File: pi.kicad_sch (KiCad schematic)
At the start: 4 parts

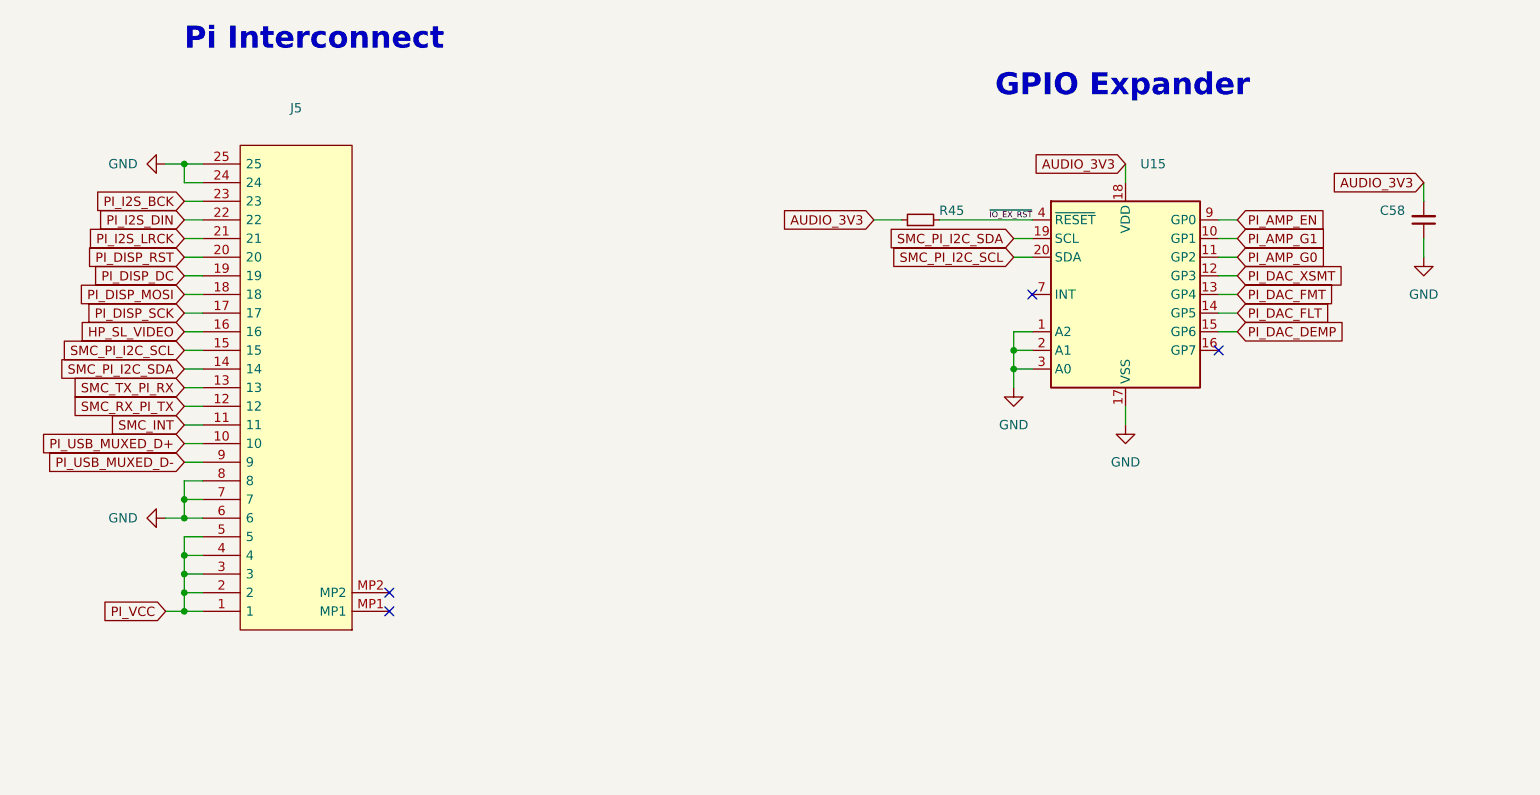
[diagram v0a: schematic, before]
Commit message: layout: add testpoints, extra mounting hole, grounding clips
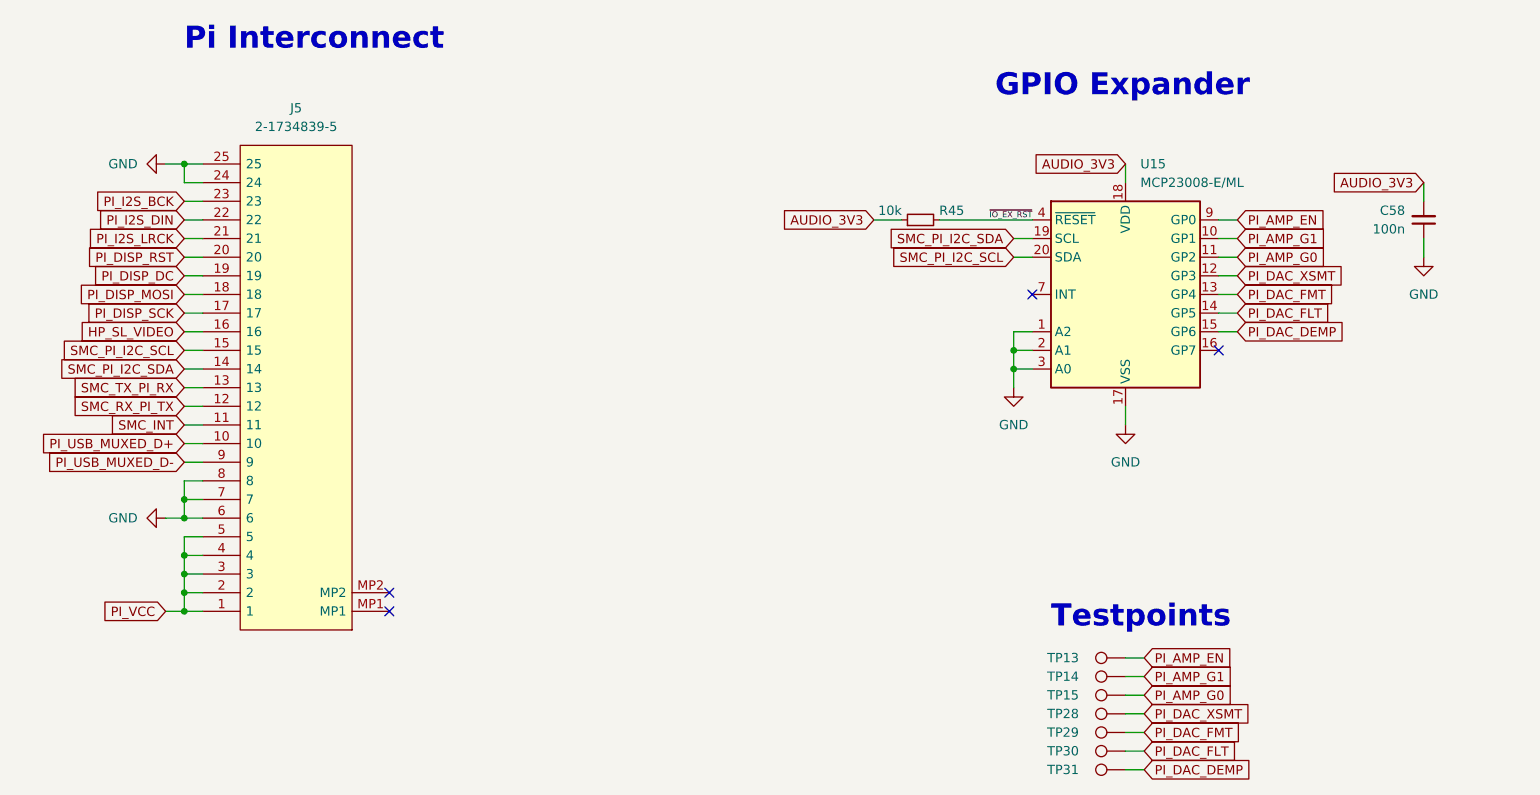
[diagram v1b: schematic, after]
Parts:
- added TP13, TP14, TP15, TP28, TP29, TP30, TP31: TestPoint, TestPoint:TestPoint_Pad_D1.5mm, symbol Connector:TestPoint
- C58: value (none) -> 100n; footprint (none) -> Capacitor_SMD:C_0402_1005Metric
- J5: value (none) -> 2-1734839-5; footprint (none) -> Gigahawk:217348395
- R45: value (none) -> 10k; footprint (none) -> Resistor_SMD:R_0402_1005Metric
- U15: value (none) -> MCP23008-E/ML; footprint (none) -> Package_DFN_QFN:QFN-20-1EP_4x4mm_P0.5mm_EP2.7x2.7mm
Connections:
- net PI_AMP_EN: now also TP13.1
- net PI_AMP_G0: now also TP15.1
- net PI_AMP_G1: now also TP14.1
- net PI_DAC_DEMP: now also TP31.1
- net PI_DAC_FLT: now also TP30.1
- net PI_DAC_FMT: now also TP29.1
- net PI_DAC_XSMT: now also TP28.1
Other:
- note added: "Testpoints"

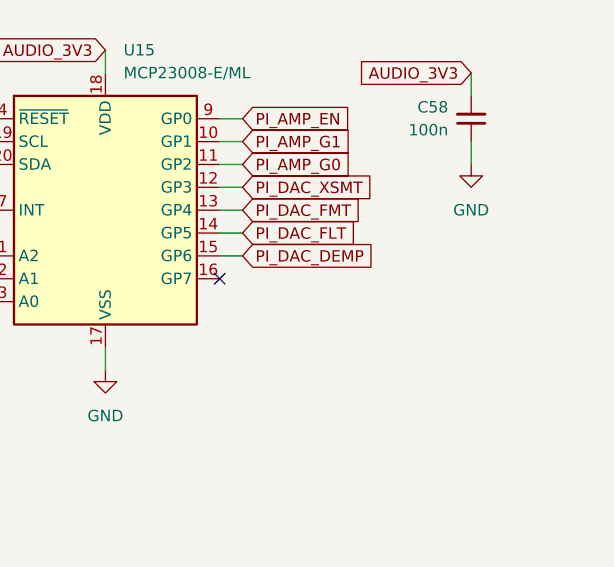
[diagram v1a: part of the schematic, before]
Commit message: schematic: add resistors to allow latching pi power
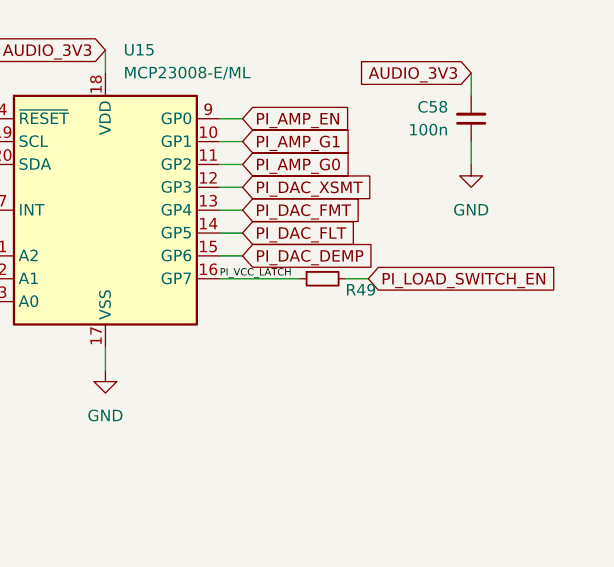
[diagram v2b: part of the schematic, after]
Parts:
- added R49: (no value), Resistor_SMD:R_0402_1005Metric, symbol Device:R_Small
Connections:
- net PI_VCC_LATCH: now reaches U15.16 (GP7)
- net PI_VCC_LATCH: now also R49.1
- new net PI_LOAD_SWITCH_EN: R49.2
- no-connect marks 4 -> 3
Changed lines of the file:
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@@
   (junction (at 40.64 69.85) (diameter 0) (color 0 0 0 0)
   )
-  (no_connect (at 181.61 95.25))
   (no_connect (at 156.21 87.63))
   (no_connect (at 68.58 130.81))
@@
     (stroke (width 0) (type default) (color 0 0 0 0))
   )
+  (wire (pts (xy 195.58 95.25) (xy 198.12 95.25))
+    (stroke (width 0) (type default) (color 0 0 0 0))
+  )
   (wire (pts (xy 43.18 123.19) (xy 40.64 123.19))
     (stroke (width 0) (type default) (color 0 0 0 0))
@@
   )
   (wire (pts (xy 40.64 85.09) (xy 43.18 85.09))
+    (stroke (width 0) (type default) (color 0 0 0 0))
+  )
+  (wire (pts (xy 181.61 95.25) (xy 190.5 95.25))
     (stroke (width 0) (type default) (color 0 0 0 0))
   )
@@
     (effects (font (size 3 3) (thickness 0.6) bold) (justify left bottom))
   )
+  (label "PI_VCC_LATCH" (at 181.61 95.25 0)
+    (effects (font (size 0.8 0.8)) (justify left bottom))
+  )
   (label "~{IO_EX_RST}" (at 156.21 77.47 180)
     (effects (font (size 0.8 0.8)) (justify right bottom))
@@
     (property "Intersheet References" "${INTERSHEET_REFS}" (id 0) (at 135.8959 80.0894 0)
       (effects (font (size 1.27 1.27)) (justify right) hide)
+    )
+  )
+  (global_label "PI_LOAD_SWITCH_EN" (shape input) (at 198.12 95.25 0) (fields_autoplaced)
+    (effects (font (size 1.27 1.27)) (justify left))
+    (property "Intersheet References" "${INTERSHEET_REFS}" (id 0) (at 219.3412 95.1706 0)
+      (effects (font (size 1.27 1.27)) (justify left) hide)
     )
   )
@@
     (pin "1")
   )
+  (symbol (lib_id "Device:R_Small") (at 193.04 95.25 90) (mirror x) (unit 1)
+    (in_bom yes) (on_board yes)
+    (property "Reference" "R49" (id 0) (at 195.58 96.52 90)
+      (effects (font (size 1.27 1.27)) (justify right))
+    )
+    (property "Value" "" (id 1) (at 190.5 96.52 90)
+      (effects (font (size 1.27 1.27)) (justify left))
+    )
+    (property "Footprint" "Resistor_SMD:R_0402_1005Metric" (id 2) (at 193.04 95.25 0)
+      (effects (font (size 1.27 1.27)) hide)
+    )
+    (property "Datasheet" "~" (id 3) (at 193.04 95.25 0)
+      (effects (font (size 1.27 1.27)) hide)
+    )
+    (pin "1")
+    (pin "2")
+  )
   (symbol (lib_id "Connector:TestPoint") (at 168.91 144.78 90) (unit 1)

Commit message: compute: finish layout and routing
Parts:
- R49: value (none) -> 1k
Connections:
- net SMC_RX_PI_TX: now also J5.13; no longer J5.12
- net SMC_TX_PI_RX: now also J5.12; no longer J5.13

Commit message: ci: prepare files for CI
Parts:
- U15: footprint Package_DFN_QFN:QFN-20-1EP_4x4mm_P0.5mm_EP2.7x2.7mm -> Gigahawk:QFN-20-1EP_4x4mm_P0.5mm_EP2.7x2.7mm
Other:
- title: (none) -> piPod IO/SMC Board
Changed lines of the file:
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@@
 (kicad_sch (version 20211123) (generator eeschema)
   (paper "A4")
+  (title_block
+    (title "piPod IO/SMC Board")
+    (date "${DATE}")
+    (rev "%{TAG} (${REVISION})")
+  )
   (junction (at 40.64 128.27) (diameter 0) (color 0 0 0 0)
   )
@@
       (effects (font (size 1.27 1.27)) (justify left))
     )
-    (property "Footprint" "Package_DFN_QFN:QFN-20-1EP_4x4mm_P0.5mm_EP2.7x2.7mm" (id 2) (at 168.91 114.3 0)
-      (effects (font (size 1.27 1.27)) hide)
-    )
+    (property "Footprint" "Gigahawk:QFN-20-1EP_4x4mm_P0.5mm_EP2.7x2.7mm" (id 2) (at 168.91 114.3 0)
+      (effects (font (size 1.27 1.27)) hide)
+    )

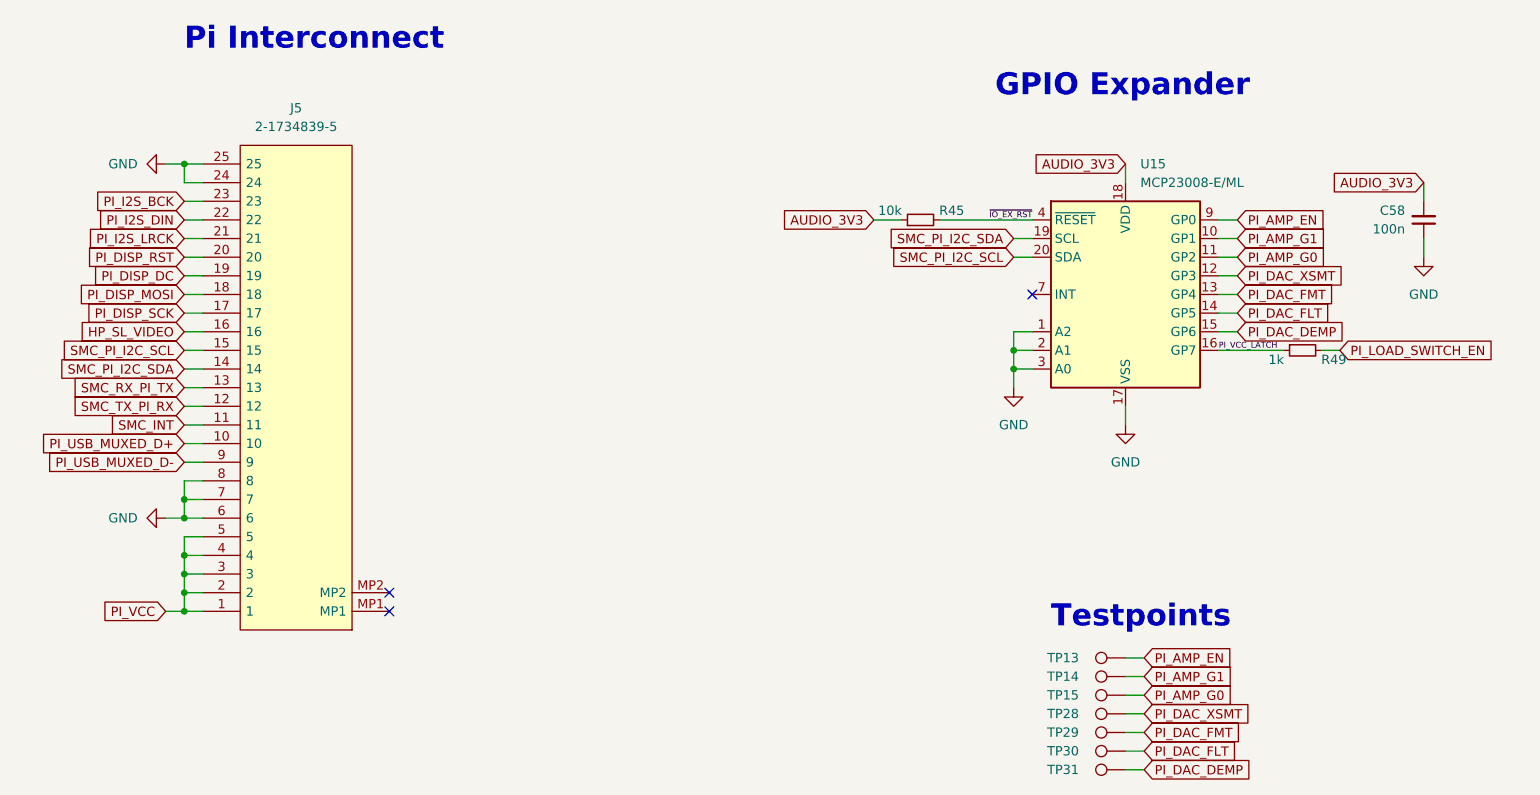
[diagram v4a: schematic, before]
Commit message: ci: test marking parts in sch for bom
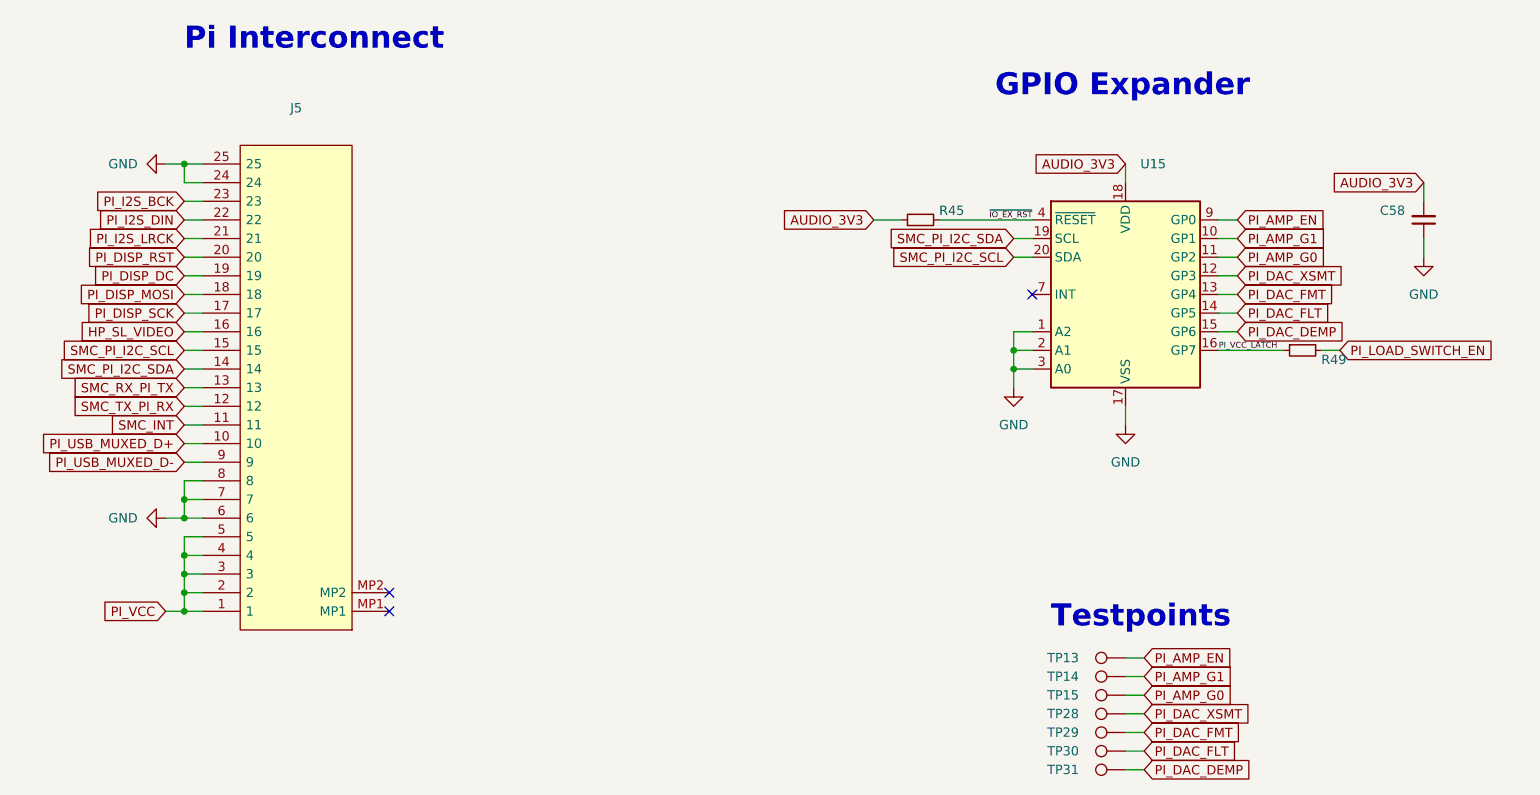
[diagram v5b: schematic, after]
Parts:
- C58: value 100n -> (none); footprint Capacitor_SMD:C_0402_1005Metric -> (none)
- J5: value 2-1734839-5 -> (none); footprint Gigahawk:217348395 -> (none)
- R45: value 10k -> (none); footprint Resistor_SMD:R_0402_1005Metric -> (none)
- R49: value 1k -> (none); footprint Resistor_SMD:R_0402_1005Metric -> (none)
- TP13, TP14, TP15, TP28, TP29, TP30, TP31: value TestPoint -> (none); footprint TestPoint:TestPoint_Pad_D1.5mm -> (none)
- U15: value MCP23008-E/ML -> (none); footprint Gigahawk:QFN-20-1EP_4x4mm_P0.5mm_EP2.7x2.7mm -> (none)
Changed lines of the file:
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@@
       (effects (font (size 1.27 1.27)) (justify right))
     )
-    (property "Value" "10k" (id 1) (at 138.43 76.2 90)
-      (effects (font (size 1.27 1.27)) (justify left))
-    )
-    (property "Footprint" "Resistor_SMD:R_0402_1005Metric" (id 2) (at 140.97 77.47 0)
+    (property "Value" "" (id 1) (at 138.43 76.2 90)
+      (effects (font (size 1.27 1.27)) (justify left))
+    )
+    (property "Footprint" "" (id 2) (at 140.97 77.47 0)
       (effects (font (size 1.27 1.27)) hide)
     )
@@
       (effects (font (size 1.27 1.27)) (justify left))
     )
-    (property "Value" "TestPoint" (id 1) (at 166.8779 147.32 0)
-      (effects (font (size 1.27 1.27)) (justify left) hide)
-    )
-    (property "Footprint" "TestPoint:TestPoint_Pad_D1.5mm" (id 2) (at 168.91 144.78 0)
+    (property "Value" "" (id 1) (at 166.8779 147.32 0)
+      (effects (font (size 1.27 1.27)) (justify left) hide)
+    )
+    (property "Footprint" "" (id 2) (at 168.91 144.78 0)
       (effects (font (size 1.27 1.27)) hide)
     )
@@
       (effects (font (size 1.27 1.27)) (justify left))
     )
-    (property "Value" "MCP23008-E/ML" (id 1) (at 170.9294 72.39 0)
-      (effects (font (size 1.27 1.27)) (justify left))
-    )
-    (property "Footprint" "Gigahawk:QFN-20-1EP_4x4mm_P0.5mm_EP2.7x2.7mm" (id 2) (at 168.91 114.3 0)
+    (property "Value" "" (id 1) (at 170.9294 72.39 0)
+      (effects (font (size 1.27 1.27)) (justify left))
+    )
+    (property "Footprint" "" (id 2) (at 168.91 114.3 0)
       (effects (font (size 1.27 1.27)) hide)
     )
@@
       (effects (font (size 1.27 1.27)) (justify left))
     )
-    (property "Value" "TestPoint" (id 1) (at 166.8779 144.78 0)
-      (effects (font (size 1.27 1.27)) (justify left) hide)
-    )
-    (property "Footprint" "TestPoint:TestPoint_Pad_D1.5mm" (id 2) (at 168.91 142.24 0)
+    (property "Value" "" (id 1) (at 166.8779 144.78 0)
+      (effects (font (size 1.27 1.27)) (justify left) hide)
+    )
+    (property "Footprint" "" (id 2) (at 168.91 142.24 0)
       (effects (font (size 1.27 1.27)) hide)
     )
@@
       (effects (font (size 1.27 1.27)) (justify left))
     )
-    (property "Value" "TestPoint" (id 1) (at 166.8779 134.62 0)
-      (effects (font (size 1.27 1.27)) (justify left) hide)
-    )
-    (property "Footprint" "TestPoint:TestPoint_Pad_D1.5mm" (id 2) (at 168.91 132.08 0)
+    (property "Value" "" (id 1) (at 166.8779 134.62 0)
+      (effects (font (size 1.27 1.27)) (justify left) hide)
+    )
+    (property "Footprint" "" (id 2) (at 168.91 132.08 0)
       (effects (font (size 1.27 1.27)) hide)
     )
@@
     (in_bom yes) (on_board yes) (fields_autoplaced)
     (property "Reference" "J5" (id 0) (at 55.88 62.23 0))
-    (property "Value" "2-1734839-5" (id 1) (at 55.88 64.77 0))
-    (property "Footprint" "Gigahawk:217348395" (id 2) (at 46.99 133.35 0)
+    (property "Value" "" (id 1) (at 55.88 64.77 0))
+    (property "Footprint" "" (id 2) (at 46.99 133.35 0)
       (effects (font (size 1.27 1.27)) (justify left) hide)
     )
@@
       (effects (font (size 1.27 1.27)) (justify right))
     )
-    (property "Value" "100n" (id 1) (at 207.01 78.7335 0)
-      (effects (font (size 1.27 1.27)) (justify right))
-    )
-    (property "Footprint" "Capacitor_SMD:C_0402_1005Metric" (id 2) (at 209.55 77.47 0)
+    (property "Value" "" (id 1) (at 207.01 78.7335 0)
+      (effects (font (size 1.27 1.27)) (justify right))
+    )
+    (property "Footprint" "" (id 2) (at 209.55 77.47 0)
       (effects (font (size 1.27 1.27)) hide)
     )
@@
       (effects (font (size 1.27 1.27)) (justify left))
     )
-    (property "Value" "TestPoint" (id 1) (at 166.8779 137.16 0)
-      (effects (font (size 1.27 1.27)) (justify left) hide)
-    )
-    (property "Footprint" "TestPoint:TestPoint_Pad_D1.5mm" (id 2) (at 168.91 134.62 0)
+    (property "Value" "" (id 1) (at 166.8779 137.16 0)
+      (effects (font (size 1.27 1.27)) (justify left) hide)
+    )
+    (property "Footprint" "" (id 2) (at 168.91 134.62 0)
       (effects (font (size 1.27 1.27)) hide)
     )
@@
       (effects (font (size 1.27 1.27)) (justify left))
     )
-    (property "Value" "TestPoint" (id 1) (at 166.8779 139.7 0)
-      (effects (font (size 1.27 1.27)) (justify left) hide)
-    )
-    (property "Footprint" "TestPoint:TestPoint_Pad_D1.5mm" (id 2) (at 168.91 137.16 0)
+    (property "Value" "" (id 1) (at 166.8779 139.7 0)
+      (effects (font (size 1.27 1.27)) (justify left) hide)
+    )
+    (property "Footprint" "" (id 2) (at 168.91 137.16 0)
       (effects (font (size 1.27 1.27)) hide)
     )
@@
       (effects (font (size 1.27 1.27)) (justify left))
     )
-    (property "Value" "TestPoint" (id 1) (at 166.8779 149.86 0)
-      (effects (font (size 1.27 1.27)) (justify left) hide)
-    )
-    (property "Footprint" "TestPoint:TestPoint_Pad_D1.5mm" (id 2) (at 168.91 147.32 0)
+    (property "Value" "" (id 1) (at 166.8779 149.86 0)
+      (effects (font (size 1.27 1.27)) (justify left) hide)
+    )
+    (property "Footprint" "" (id 2) (at 168.91 147.32 0)
       (effects (font (size 1.27 1.27)) hide)
     )
@@
       (effects (font (size 1.27 1.27)) (justify right))
     )
-    (property "Value" "1k" (id 1) (at 190.5 96.52 90)
-      (effects (font (size 1.27 1.27)) (justify left))
-    )
-    (property "Footprint" "Resistor_SMD:R_0402_1005Metric" (id 2) (at 193.04 95.25 0)
+    (property "Value" "" (id 1) (at 190.5 96.52 90)
+      (effects (font (size 1.27 1.27)) (justify left))
+    )
+    (property "Footprint" "" (id 2) (at 193.04 95.25 0)
       (effects (font (size 1.27 1.27)) hide)
     )
@@
       (effects (font (size 1.27 1.27)) (justify left))
     )
-    (property "Value" "TestPoint" (id 1) (at 166.8779 142.24 0)
-      (effects (font (size 1.27 1.27)) (justify left) hide)
-    )
-    (property "Footprint" "TestPoint:TestPoint_Pad_D1.5mm" (id 2) (at 168.91 139.7 0)
-      (effects (font (size 1.27 1.27)) hide)
-    )
+    (property "Value" "" (id 1) (at 166.8779 142.24 0)
+      (effects (font (size 1.27 1.27)) (justify left) hide)
+    )
+    (property "Footprint" "" (id 2) (at 168.91 139.7 0)
+      (effects (font (size 1.27 1.27)) hide)
+    )
